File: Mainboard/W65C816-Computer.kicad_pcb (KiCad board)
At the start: 2 copper layers, 93 parts, among them J1 ADDR_DATA_DBG, J2 CTRL_BANK_DBG, J3 CPU_MISC_DBG, J4 PJ-102A, J5 DAUGHTER_PWR_AUX, J6 DAUGHTER_BUS_A, J7 DAUGHTER_BUS_B, Q1 P-MOSFET_REV_PROT_TO220, SW1 RESET, SW2 NMI, SW3 MAIN_PWR_SW_EXT, U1 W65C816S6PG-14, U10 SN74HC04N, U2 SN74HC573N, U20 AS6C4008-55PCN, U21 AS6C4008-55PCN, U22 AS6C4008-55PCN, U23 AS6C4008-55PCN, U24 AS6C4008-55PCN, U25 AS6C4008-55PCN, U26 AS6C4008-55PCN, U27 AS6C4008-55PCN, U3 SN74HC245N, U30 SST39VF040-70-4I-NHE, U4 MCP130-315D, U5 SN74HC14N, U6 SN74HC138N, U7 SN74HC138N, U9 SN74HC00N, X1 ECS-P143X-8.000-BN

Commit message: Add lock file for W65C816-Computer project with hostname and username
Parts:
- moved J6 198.0 mm to (322.2, -24.3)
- moved J7 163.9 mm to (315.0, -24.3)

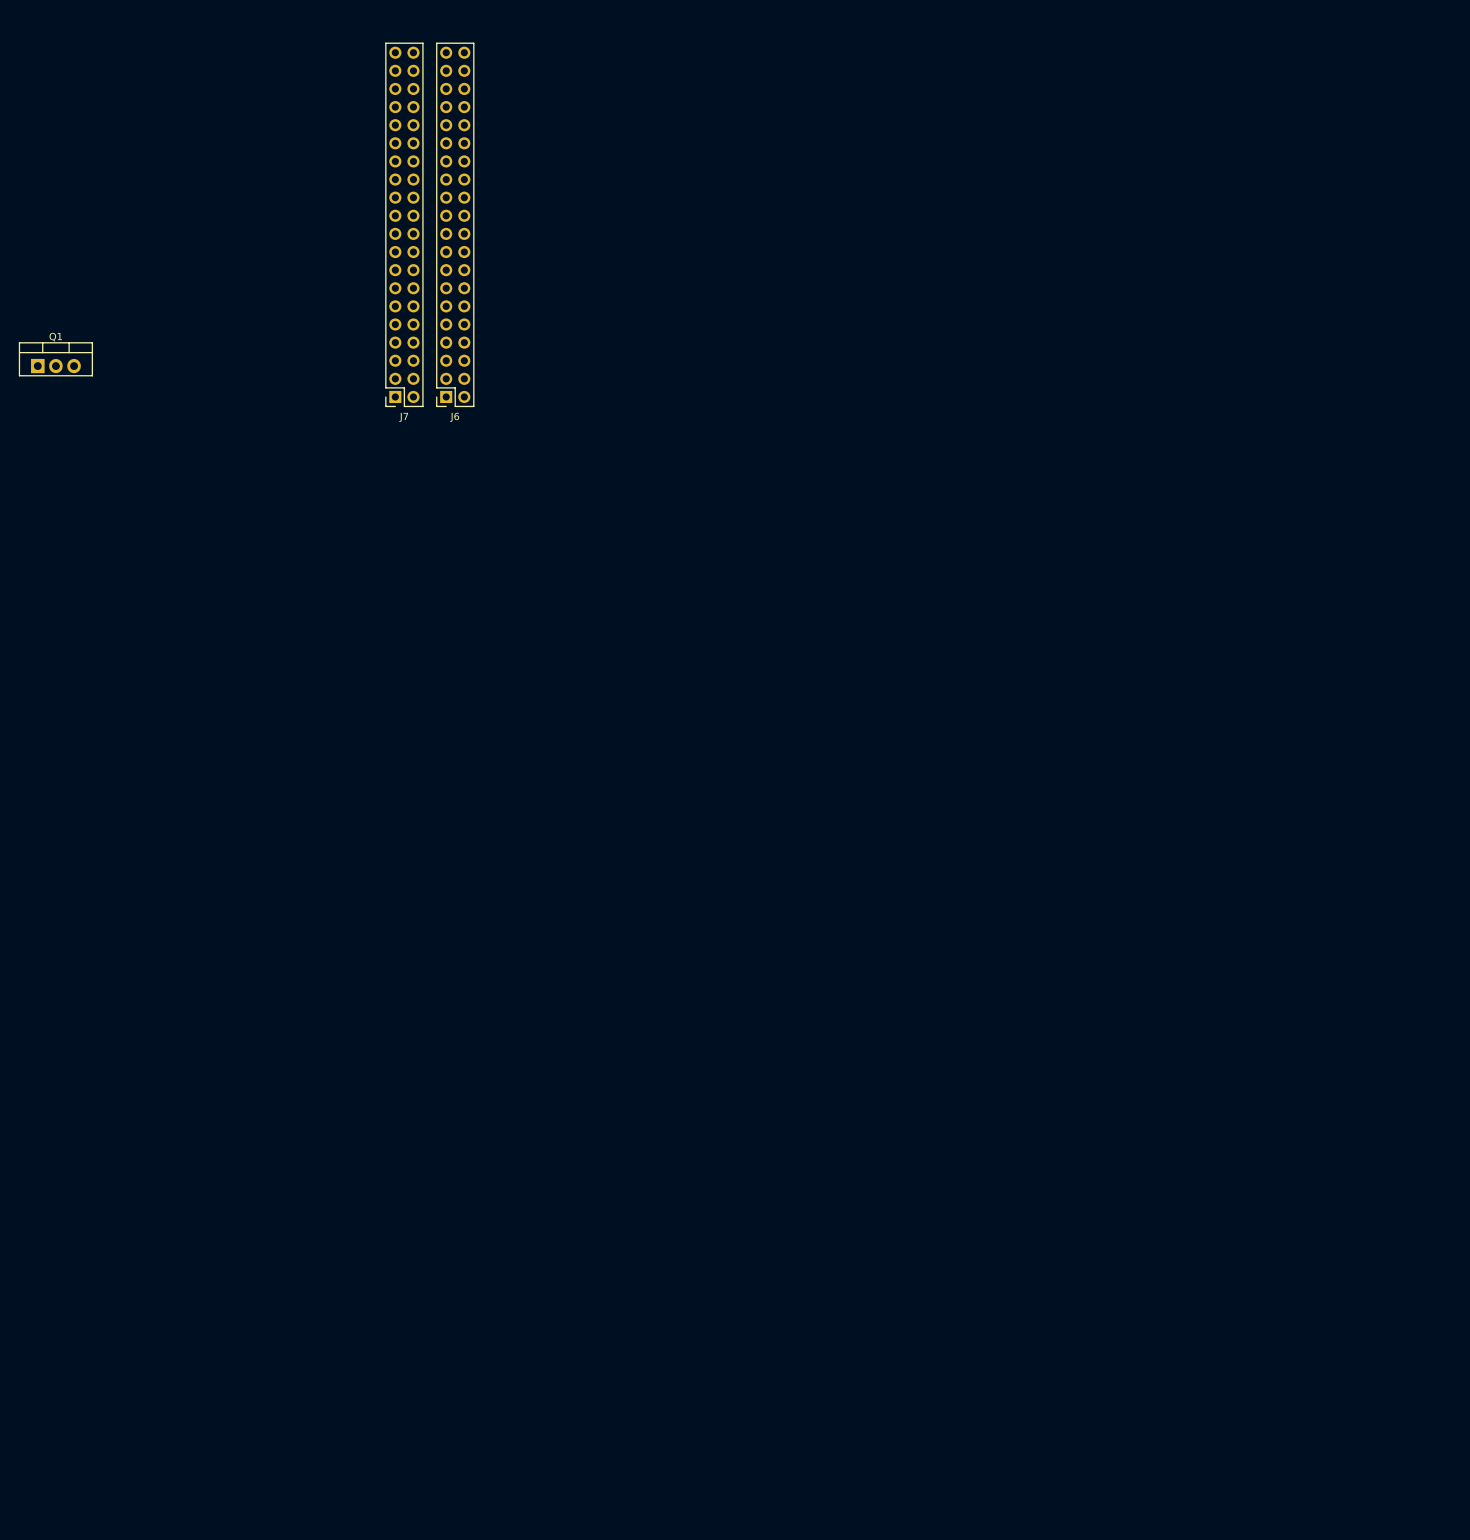
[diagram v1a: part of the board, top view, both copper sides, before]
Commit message: Add CardEdge EDAC 395 footprint and update library table
- Created a new footprint for the CardEdge EDAC 395 2x40 P2.54mm Vertical THT connector in the W65C816-Computer.pretty library.
- Added the footprint to the fp-lib-table for easy access in KiCad.
- Documented the W65C816/RP2350 interface plan, outlining architecture, memory mapping, data bus contracts, interrupt architecture, and implementation sequence for revision A.
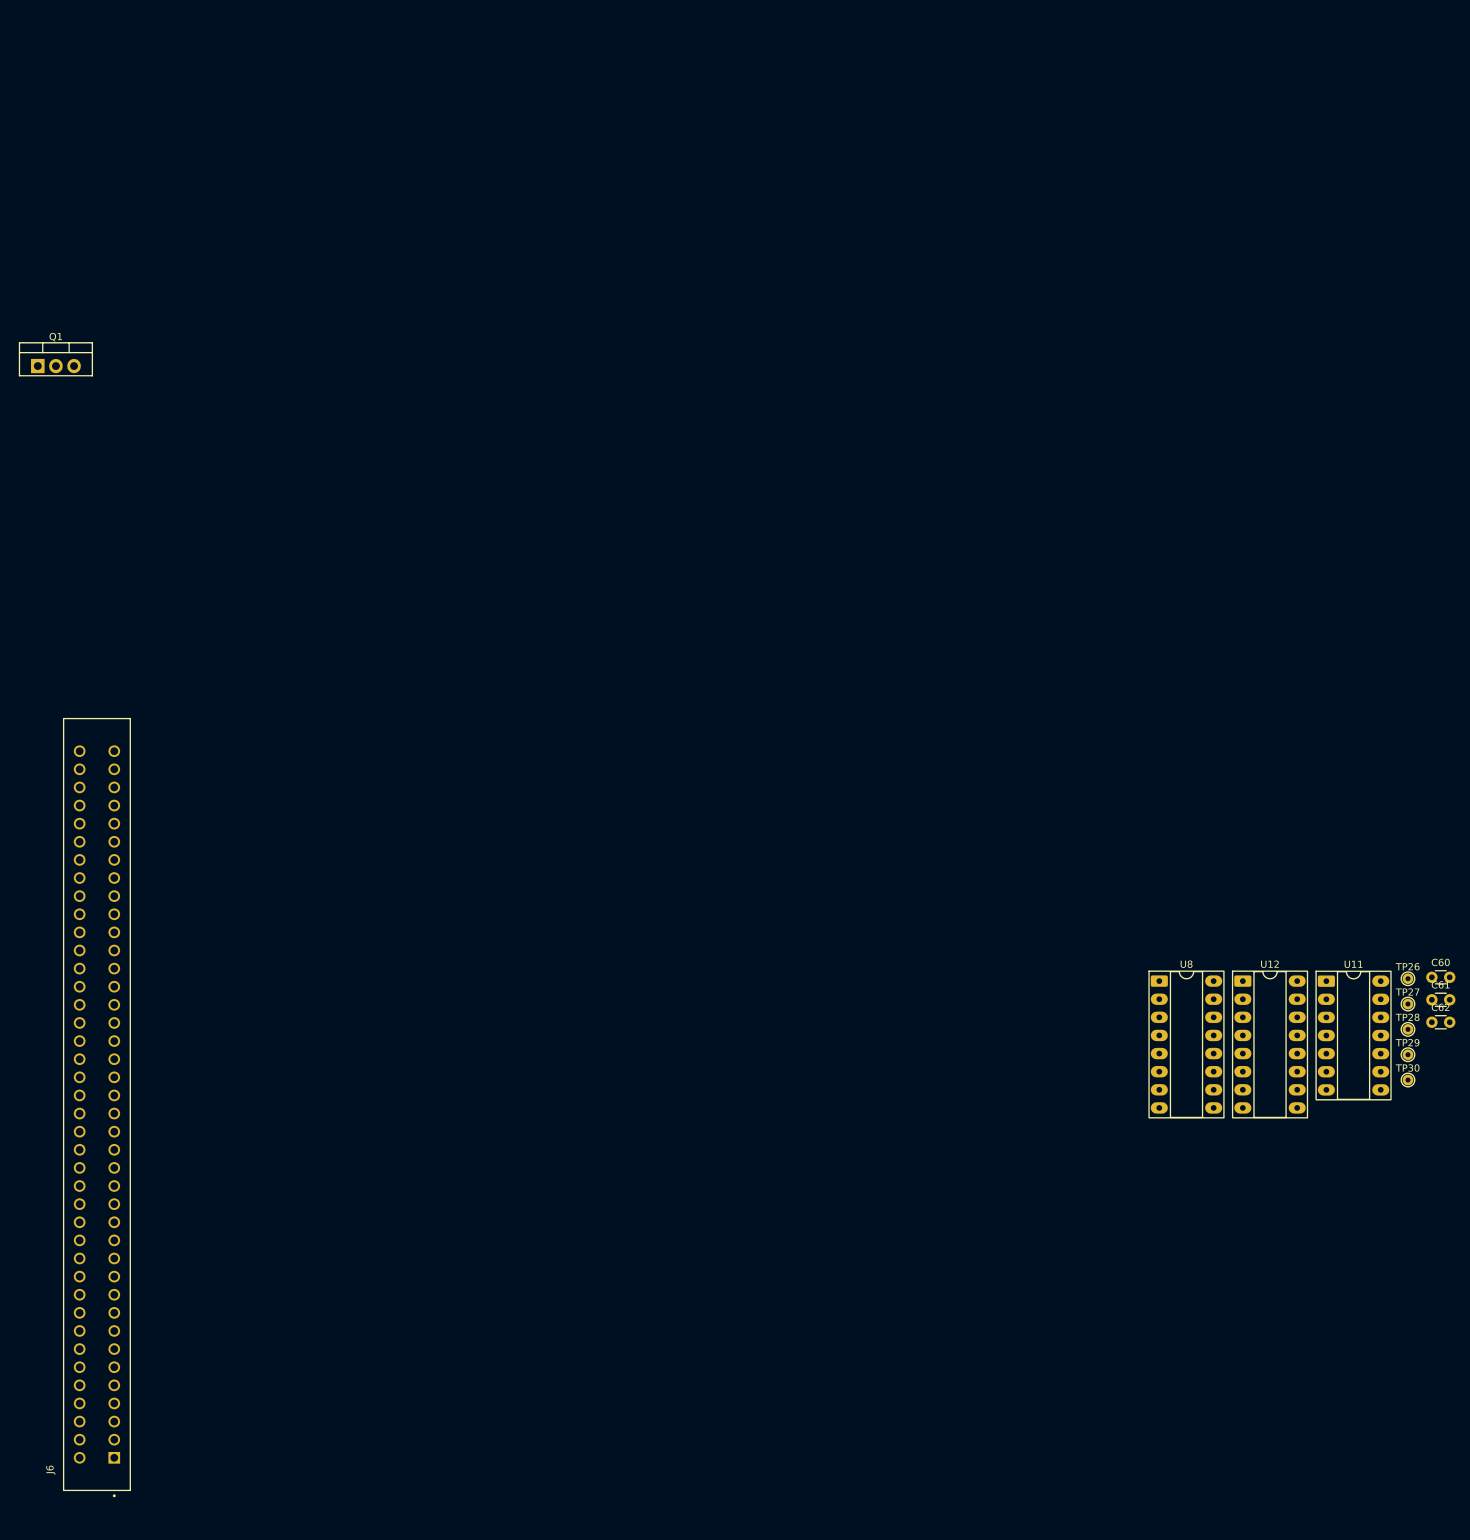
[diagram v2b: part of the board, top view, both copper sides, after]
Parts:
- removed J7: DAUGHTER_BUS_B, Connector_PinSocket_2.54mm:PinSocket_2x20_P2.54mm_Vertical
- added C60: 100nF, Capacitor_THT:C_Disc_D3.0mm_W1.6mm_P2.50mm, F.Cu at (460.4, 57.0)
- added C61: 100nF, Capacitor_THT:C_Disc_D3.0mm_W1.6mm_P2.50mm, F.Cu at (460.4, 60.2)
- added C62: 100nF, Capacitor_THT:C_Disc_D3.0mm_W1.6mm_P2.50mm, F.Cu at (460.4, 63.3)
- added TP26: RP_CS_N, TestPoint:TestPoint_THTPad_D1.5mm_Drill0.7mm, F.Cu at (457.0, 57.2)
- added TP27: IO_CS_N, TestPoint:TestPoint_THTPad_D1.5mm_Drill0.7mm, F.Cu at (457.0, 60.8)
- added TP28: EXP_CS_N, TestPoint:TestPoint_THTPad_D1.5mm_Drill0.7mm, F.Cu at (457.0, 64.3)
- added TP29: IO_RD_N, TestPoint:TestPoint_THTPad_D1.5mm_Drill0.7mm, F.Cu at (457.0, 67.9)
- added TP30: IO_WR_N, TestPoint:TestPoint_THTPad_D1.5mm_Drill0.7mm, F.Cu at (457.0, 71.4)
- added U11: SN74HC08N, Package_DIP:DIP-14_W7.62mm_Socket_LongPads, F.Cu at (445.6, 57.6)
- added U12: SN74HC139N, Package_DIP:DIP-16_W7.62mm_Socket_LongPads, F.Cu at (433.9, 57.6)
- added U8: SN74HC138N, Package_DIP:DIP-16_W7.62mm_Socket_LongPads, F.Cu at (422.1, 57.6)
- J6: value DAUGHTER_BUS_A -> DAUGHTER_CARD_EDGE; footprint Connector_PinSocket_2.54mm:PinSocket_2x20_P2.54mm_Vertical -> 80_Standard_Edge_Conn:TE_2-5530843-0
- moved J6 110.6 mm to (273.2, 74.9), turned to 90 degrees

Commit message: Add ISA16 Slot footprint and mainboard PCB file
- Introduced a new footprint for the ISA16 Slot, including detailed pad specifications and dimensions.
- Added the W65C816-Computer.kicad_pcb.zip file containing the mainboard PCB design.
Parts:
- removed C1, C10, C11, C12, C2, C20, C21, C22, C23, C24, C25, C26, C27, C3, C30, C4, C41, C43, C5, C60, C61, C62, C7, C8, C9: 100nF, Capacitor_THT:C_Disc_D3.0mm_W1.6mm_P2.50mm
- removed C40, C42: 470uF, Capacitor_THT:CP_Radial_D8.0mm_P5.00mm
- removed C6: 10uF, Capacitor_THT:C_Disc_D5.0mm_W2.5mm_P2.50mm
- removed D1: P6KE5.0A, Diode_THT:D_DO-15_P10.16mm_Horizontal
- removed F1: 5A, Fuse:Fuseholder_Clip-5x20mm_Littelfuse_111_Inline_P20.00x5.00mm_D1.05mm_Horizontal
- removed J1: ADDR_DATA_DBG, Connector_PinHeader_2.54mm:PinHeader_1x20_P2.54mm_Vertical
- removed J2: CTRL_BANK_DBG, Connector_PinHeader_2.54mm:PinHeader_1x20_P2.54mm_Vertical
- removed J3: CPU_MISC_DBG, Connector_PinHeader_2.54mm:PinHeader_1x10_P2.54mm_Vertical
- removed J4: PJ-102A, PJ-102A:CUI_PJ-102A
- removed J5: DAUGHTER_PWR_AUX, Connector_PinSocket_2.54mm:PinSocket_1x06_P2.54mm_Vertical
- removed J6: DAUGHTER_CARD_EDGE, 80_Standard_Edge_Conn:TE_2-5530843-0
- removed JP1: FLASH_WE_EN, Connector_PinHeader_2.54mm:PinHeader_1x02_P2.54mm_Vertical
- removed LED1: PWR, LED_THT:LED_D5.0mm
- removed MOD1: 3V3_BUCK_MODULE_5V_IN_3A, Connector_PinSocket_2.54mm:PinSocket_1x04_P2.54mm_Vertical
- removed Q1: P-MOSFET_REV_PROT_TO220, Package_TO_SOT_THT:TO-220-3_Vertical
- removed R1, R2, R3, R30, R4, R5, R6: 10k, Resistor_THT:R_Axial_DIN0207_L6.3mm_D2.5mm_P7.62mm_Horizontal
- removed R41: 1k, Resistor_THT:R_Axial_DIN0207_L6.3mm_D2.5mm_P7.62mm_Horizontal
- removed SW1: RESET, Button_Switch_THT:SW_PUSH_6mm_H4.3mm
- removed SW2: NMI, Button_Switch_THT:SW_PUSH_6mm_H4.3mm
- removed SW3: MAIN_PWR_SW_EXT, TerminalBlock_RND:TerminalBlock_RND_205-00232_1x02_P5.08mm_Horizontal
- removed TP1: PHI2, TestPoint:TestPoint_THTPad_D1.5mm_Drill0.7mm
- removed TP10: ABORT_N, TestPoint:TestPoint_THTPad_D1.5mm_Drill0.7mm
- removed TP11: PHI2_N, TestPoint:TestPoint_THTPad_D1.5mm_Drill0.7mm
- removed TP12: RAM_CS0_N, TestPoint:TestPoint_THTPad_D1.5mm_Drill0.7mm
- removed TP13: RAM_CS1_N, TestPoint:TestPoint_THTPad_D1.5mm_Drill0.7mm
- removed TP14: RAM_CS2_N, TestPoint:TestPoint_THTPad_D1.5mm_Drill0.7mm
- removed TP15: RAM_CS3_N, TestPoint:TestPoint_THTPad_D1.5mm_Drill0.7mm
- removed TP16: RAM_CS4_N, TestPoint:TestPoint_THTPad_D1.5mm_Drill0.7mm
- removed TP17: RAM_CS5_N, TestPoint:TestPoint_THTPad_D1.5mm_Drill0.7mm
- removed TP18: RAM_CS6_N, TestPoint:TestPoint_THTPad_D1.5mm_Drill0.7mm
- removed TP19: RAM_CS7_N, TestPoint:TestPoint_THTPad_D1.5mm_Drill0.7mm
- removed TP2: RESET_N, TestPoint:TestPoint_THTPad_D1.5mm_Drill0.7mm
- removed TP20: ROM_CS_N, TestPoint:TestPoint_THTPad_D1.5mm_Drill0.7mm
- removed TP21: MEM_OE_N, TestPoint:TestPoint_THTPad_D1.5mm_Drill0.7mm
- removed TP22: MEM_WE_N, TestPoint:TestPoint_THTPad_D1.5mm_Drill0.7mm
- removed TP23: +5V, TestPoint:TestPoint_THTPad_D1.5mm_Drill0.7mm
- removed TP24: +3V3, TestPoint:TestPoint_THTPad_D1.5mm_Drill0.7mm
- removed TP25: GND, TestPoint:TestPoint_THTPad_D1.5mm_Drill0.7mm
- removed TP26: RP_CS_N, TestPoint:TestPoint_THTPad_D1.5mm_Drill0.7mm
- removed TP27: IO_CS_N, TestPoint:TestPoint_THTPad_D1.5mm_Drill0.7mm
- removed TP28: EXP_CS_N, TestPoint:TestPoint_THTPad_D1.5mm_Drill0.7mm
- removed TP29: IO_RD_N, TestPoint:TestPoint_THTPad_D1.5mm_Drill0.7mm
- removed TP3: IRQ_N, TestPoint:TestPoint_THTPad_D1.5mm_Drill0.7mm
- removed TP30: IO_WR_N, TestPoint:TestPoint_THTPad_D1.5mm_Drill0.7mm
- removed TP4: NMI_N, TestPoint:TestPoint_THTPad_D1.5mm_Drill0.7mm
- removed TP5: RDY, TestPoint:TestPoint_THTPad_D1.5mm_Drill0.7mm
- removed TP6: RWB, TestPoint:TestPoint_THTPad_D1.5mm_Drill0.7mm
- removed TP7: VDA, TestPoint:TestPoint_THTPad_D1.5mm_Drill0.7mm
- removed TP8: VPA, TestPoint:TestPoint_THTPad_D1.5mm_Drill0.7mm
- removed TP9: BE, TestPoint:TestPoint_THTPad_D1.5mm_Drill0.7mm
- removed U1: W65C816S6PG-14, Package_DIP:DIP-40_W15.24mm_Socket_LongPads
- removed U10: SN74HC04N, Package_DIP:DIP-14_W7.62mm_Socket_LongPads
- removed U11: SN74HC08N, Package_DIP:DIP-14_W7.62mm_Socket_LongPads
- removed U12: SN74HC139N, Package_DIP:DIP-16_W7.62mm_Socket_LongPads
- removed U2: SN74HC573N, Package_DIP:DIP-20_W7.62mm_Socket_LongPads
- removed U20, U21, U22, U23, U24, U25, U26, U27: AS6C4008-55PCN, Package_DIP:DIP-32_W15.24mm_Socket_LongPads
- removed U3: SN74HC245N, Package_DIP:DIP-20_W7.62mm_Socket_LongPads
- removed U30: SST39VF040-70-4I-NHE, Package_LCC:PLCC-32_THT-Socket
- removed U4: MCP130-315D, Package_TO_SOT_THT:TO-92_Inline
- removed U5: SN74HC14N, Package_DIP:DIP-14_W7.62mm_Socket_LongPads
- removed U6, U7, U8: SN74HC138N, Package_DIP:DIP-16_W7.62mm_Socket_LongPads
- removed U9: SN74HC00N, Package_DIP:DIP-14_W7.62mm_Socket_LongPads
- removed X1: ECS-P143X-8.000-BN, Oscillator:Oscillator_DIP-14
- added H1: MountingHole, MountingHole:MountingHole_4.3mm_M4_Pad_Via, F.Cu at (32.7, 183.7)
- added H2: MountingHole, MountingHole:MountingHole_4.3mm_M4_Pad_Via, F.Cu at (187.7, 183.7)
- added H3: MountingHole, MountingHole:MountingHole_4.3mm_M4_Pad_Via, F.Cu at (187.7, 26.2)
- added H4: MountingHole, MountingHole:MountingHole_4.3mm_M4_Pad_Via, F.Cu at (55.6, 26.2)
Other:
- board outline added: 170 x 170 mm
- board text added: "@Sulfuroid"
- board text added: "BACK"
- board text added: "MINI-ITX Kicad Template"

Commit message: Added 4MiB memory back
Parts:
- added C1: 100nF, Capacitor_THT:C_Disc_D3.0mm_W1.6mm_P2.50mm, F.Cu at (338.2, -90.4)
- added C10: 100nF, Capacitor_THT:C_Disc_D3.0mm_W1.6mm_P2.50mm, F.Cu at (343.9, -87.3)
- added C11: 100nF, Capacitor_THT:C_Disc_D3.0mm_W1.6mm_P2.50mm, F.Cu at (343.9, -84.1)
- added C12: 100nF, Capacitor_THT:C_Disc_D3.0mm_W1.6mm_P2.50mm, F.Cu at (343.9, -81.0)
- added C2: 100nF, Capacitor_THT:C_Disc_D3.0mm_W1.6mm_P2.50mm, F.Cu at (338.2, -87.3)
- added C20: 100nF, Capacitor_THT:C_Disc_D3.0mm_W1.6mm_P2.50mm, F.Cu at (343.9, -77.8)
- added C21: 100nF, Capacitor_THT:C_Disc_D3.0mm_W1.6mm_P2.50mm, F.Cu at (343.9, -74.7)
- added C22: 100nF, Capacitor_THT:C_Disc_D3.0mm_W1.6mm_P2.50mm, F.Cu at (343.9, -71.5)
- added C23: 100nF, Capacitor_THT:C_Disc_D3.0mm_W1.6mm_P2.50mm, F.Cu at (349.5, -90.4)
- added C24: 100nF, Capacitor_THT:C_Disc_D3.0mm_W1.6mm_P2.50mm, F.Cu at (294.3, -14.2)
- added C25: 100nF, Capacitor_THT:C_Disc_D3.0mm_W1.6mm_P2.50mm, F.Cu at (349.5, -84.1)
- added C26: 100nF, Capacitor_THT:C_Disc_D3.0mm_W1.6mm_P2.50mm, F.Cu at (349.5, -81.0)
- added C27: 100nF, Capacitor_THT:C_Disc_D3.0mm_W1.6mm_P2.50mm, F.Cu at (349.5, -77.8)
- added C3: 100nF, Capacitor_THT:C_Disc_D3.0mm_W1.6mm_P2.50mm, F.Cu at (338.2, -84.1)
- added C30: 100nF, Capacitor_THT:C_Disc_D3.0mm_W1.6mm_P2.50mm, F.Cu at (349.5, -74.7)
- added C4: 100nF, Capacitor_THT:C_Disc_D3.0mm_W1.6mm_P2.50mm, F.Cu at (338.2, -81.0)
- added C40: 470uF, Capacitor_THT:CP_Radial_D8.0mm_P5.00mm, F.Cu at (361.7, -87.2)
- added C41: 100nF, Capacitor_THT:C_Disc_D3.0mm_W1.6mm_P2.50mm, F.Cu at (349.5, -71.5)
- added C42: 470uF, Capacitor_THT:CP_Radial_D8.0mm_P5.00mm, F.Cu at (361.7, -77.7)
- added C43: 100nF, Capacitor_THT:C_Disc_D3.0mm_W1.6mm_P2.50mm, F.Cu at (355.2, -90.4)
- added C5: 100nF, Capacitor_THT:C_Disc_D3.0mm_W1.6mm_P2.50mm, F.Cu at (338.2, -77.8)
- added C6: 10uF, Capacitor_THT:C_Disc_D5.0mm_W2.5mm_P2.50mm, F.Cu at (363.5, -37.8)
- added C60: 100nF, Capacitor_THT:C_Disc_D3.0mm_W1.6mm_P2.50mm, F.Cu at (355.2, -87.3)
- added C61: 100nF, Capacitor_THT:C_Disc_D3.0mm_W1.6mm_P2.50mm, F.Cu at (355.2, -84.1)
- added C62: 100nF, Capacitor_THT:C_Disc_D3.0mm_W1.6mm_P2.50mm, F.Cu at (355.2, -81.0)
- added C7: 100nF, Capacitor_THT:C_Disc_D3.0mm_W1.6mm_P2.50mm, F.Cu at (338.2, -74.7)
- added C8: 100nF, Capacitor_THT:C_Disc_D3.0mm_W1.6mm_P2.50mm, F.Cu at (338.2, -71.5)
- added C9: 100nF, Capacitor_THT:C_Disc_D3.0mm_W1.6mm_P2.50mm, F.Cu at (343.9, -90.4)
- added D1: P6KE5.0A, Diode_THT:D_DO-15_P10.16mm_Horizontal, F.Cu at (349.4, -44.7)
- added F1: 5A, Fuse:Fuseholder_Clip-5x20mm_Littelfuse_111_Inline_P20.00x5.00mm_D1.05mm_Horizontal, F.Cu at (279.3, -41.3)
- added J1: ADDR_DATA_DBG, Connector_PinHeader_2.54mm:PinHeader_1x20_P2.54mm_Vertical, F.Cu at (329.7, -116.7)
- added J2: CTRL_BANK_DBG, Connector_PinHeader_2.54mm:PinHeader_1x20_P2.54mm_Vertical, F.Cu at (334.3, -116.7)
- added J3: CPU_MISC_DBG, Connector_PinHeader_2.54mm:PinHeader_1x10_P2.54mm_Vertical, F.Cu at (329.7, -63.9)
- added J4: PJ-102A, PJ-102A:CUI_PJ-102A, F.Cu at (314.6, -55.0)
- added J5: DAUGHTER_PWR_AUX, Connector_PinSocket_2.54mm:PinSocket_1x06_P2.54mm_Vertical, F.Cu at (334.3, -63.9)
- added J6: ISA16_DAUGHTER_BUS, W65C816_Connector:ISA16_Slot, F.Cu at (110.6, 181.4)
- added JP1: FLASH_WE_EN, Connector_PinHeader_2.54mm:PinHeader_1x02_P2.54mm_Vertical, F.Cu at (303.4, -42.4)
- added LED1: PWR, LED_THT:LED_D5.0mm, F.Cu at (364.0, -43.5)
- added MOD1: 3V3_BUCK_MODULE_5V_IN_3A, Connector_PinSocket_2.54mm:PinSocket_1x04_P2.54mm_Vertical, F.Cu at (322.6, -47.7)
- added Q1: P-MOSFET_REV_PROT_TO220, Package_TO_SOT_THT:TO-220-3_Vertical, F.Cu at (350.6, -38.2)
- added R1: 10k, Resistor_THT:R_Axial_DIN0207_L6.3mm_D2.5mm_P7.62mm_Horizontal, F.Cu at (338.2, -67.9)
- added R2: 10k, Resistor_THT:R_Axial_DIN0207_L6.3mm_D2.5mm_P7.62mm_Horizontal, F.Cu at (338.2, -63.9)
- added R3: 10k, Resistor_THT:R_Axial_DIN0207_L6.3mm_D2.5mm_P7.62mm_Horizontal, F.Cu at (338.2, -59.8)
- added R30: 10k, Resistor_THT:R_Axial_DIN0207_L6.3mm_D2.5mm_P7.62mm_Horizontal, F.Cu at (338.2, -43.6)
- added R4: 10k, Resistor_THT:R_Axial_DIN0207_L6.3mm_D2.5mm_P7.62mm_Horizontal, F.Cu at (338.2, -55.8)
- added R41: 1k, Resistor_THT:R_Axial_DIN0207_L6.3mm_D2.5mm_P7.62mm_Horizontal, F.Cu at (338.2, -39.6)
- added R5: 10k, Resistor_THT:R_Axial_DIN0207_L6.3mm_D2.5mm_P7.62mm_Horizontal, F.Cu at (338.2, -51.7)
- added R6: 10k, Resistor_THT:R_Axial_DIN0207_L6.3mm_D2.5mm_P7.62mm_Horizontal, F.Cu at (338.2, -47.7)
- added SW1: RESET, Button_Switch_THT:SW_PUSH_6mm_H4.3mm, F.Cu at (362.1, -117.0)
- added SW2: NMI, Button_Switch_THT:SW_PUSH_6mm_H4.3mm, F.Cu at (362.1, -108.5)
- added SW3: MAIN_PWR_SW_EXT, TerminalBlock_RND:TerminalBlock_RND_205-00232_1x02_P5.08mm_Horizontal, F.Cu at (311.7, -44.6)
- added TP1: PHI2, TestPoint:TestPoint_THTPad_D1.5mm_Drill0.7mm, F.Cu at (279.3, -74.9)
- added TP10: ABORT_N, TestPoint:TestPoint_THTPad_D1.5mm_Drill0.7mm, F.Cu at (282.9, -60.7)
- added TP11: PHI2_N, TestPoint:TestPoint_THTPad_D1.5mm_Drill0.7mm, F.Cu at (286.4, -74.9)
- added TP12: RAM_CS0_N, TestPoint:TestPoint_THTPad_D1.5mm_Drill0.7mm, F.Cu at (286.4, -71.4)
- added TP13: RAM_CS1_N, TestPoint:TestPoint_THTPad_D1.5mm_Drill0.7mm, F.Cu at (286.4, -67.8)
- added TP14: RAM_CS2_N, TestPoint:TestPoint_THTPad_D1.5mm_Drill0.7mm, F.Cu at (286.4, -64.3)
- added TP15: RAM_CS3_N, TestPoint:TestPoint_THTPad_D1.5mm_Drill0.7mm, F.Cu at (286.4, -60.7)
- added TP16: RAM_CS4_N, TestPoint:TestPoint_THTPad_D1.5mm_Drill0.7mm, F.Cu at (290.0, -74.9)
- added TP17: RAM_CS5_N, TestPoint:TestPoint_THTPad_D1.5mm_Drill0.7mm, F.Cu at (290.0, -71.4)
- added TP18: RAM_CS6_N, TestPoint:TestPoint_THTPad_D1.5mm_Drill0.7mm, F.Cu at (290.0, -67.8)
- added TP19: RAM_CS7_N, TestPoint:TestPoint_THTPad_D1.5mm_Drill0.7mm, F.Cu at (290.0, -64.3)
- added TP2: RESET_N, TestPoint:TestPoint_THTPad_D1.5mm_Drill0.7mm, F.Cu at (279.3, -71.4)
- added TP20: ROM_CS_N, TestPoint:TestPoint_THTPad_D1.5mm_Drill0.7mm, F.Cu at (290.0, -60.7)
- added TP21: MEM_OE_N, TestPoint:TestPoint_THTPad_D1.5mm_Drill0.7mm, F.Cu at (293.5, -74.9)
- added TP22: MEM_WE_N, TestPoint:TestPoint_THTPad_D1.5mm_Drill0.7mm, F.Cu at (293.5, -71.4)
- added TP23: +5V, TestPoint:TestPoint_THTPad_D1.5mm_Drill0.7mm, F.Cu at (293.5, -67.8)
- added TP24: +3V3, TestPoint:TestPoint_THTPad_D1.5mm_Drill0.7mm, F.Cu at (293.5, -64.3)
- added TP25: GND, TestPoint:TestPoint_THTPad_D1.5mm_Drill0.7mm, F.Cu at (293.5, -60.7)
- added TP26: RP_CS_N, TestPoint:TestPoint_THTPad_D1.5mm_Drill0.7mm, F.Cu at (297.1, -74.9)
- added TP27: IO_CS_N, TestPoint:TestPoint_THTPad_D1.5mm_Drill0.7mm, F.Cu at (297.1, -71.4)
- added TP28: EXP_CS_N, TestPoint:TestPoint_THTPad_D1.5mm_Drill0.7mm, F.Cu at (297.1, -67.8)
- added TP29: IO_RD_N, TestPoint:TestPoint_THTPad_D1.5mm_Drill0.7mm, F.Cu at (297.1, -64.3)
- added TP3: IRQ_N, TestPoint:TestPoint_THTPad_D1.5mm_Drill0.7mm, F.Cu at (279.3, -67.8)
- added TP30: IO_WR_N, TestPoint:TestPoint_THTPad_D1.5mm_Drill0.7mm, F.Cu at (297.1, -60.7)
- added TP4: NMI_N, TestPoint:TestPoint_THTPad_D1.5mm_Drill0.7mm, F.Cu at (279.3, -64.3)
- added TP5: RDY, TestPoint:TestPoint_THTPad_D1.5mm_Drill0.7mm, F.Cu at (279.3, -60.7)
- added TP6: RWB, TestPoint:TestPoint_THTPad_D1.5mm_Drill0.7mm, F.Cu at (282.9, -74.9)
- added TP7: VDA, TestPoint:TestPoint_THTPad_D1.5mm_Drill0.7mm, F.Cu at (282.9, -71.4)
- added TP8: VPA, TestPoint:TestPoint_THTPad_D1.5mm_Drill0.7mm, F.Cu at (282.9, -67.8)
- added TP9: BE, TestPoint:TestPoint_THTPad_D1.5mm_Drill0.7mm, F.Cu at (282.9, -64.3)
- added U1: W65C816S6PG-14, Package_DIP:DIP-40_W15.24mm_Socket_LongPads, F.Cu at (134.7, 83.7)
- added U10: SN74HC04N, Package_DIP:DIP-14_W7.62mm_Socket_LongPads, F.Cu at (256.2, -52.6)
- added U11: SN74HC08N, Package_DIP:DIP-14_W7.62mm_Socket_LongPads, F.Cu at (267.9, -52.6)
- added U12: SN74HC139N, Package_DIP:DIP-16_W7.62mm_Socket_LongPads, F.Cu at (267.9, -74.6)
- added U2: SN74HC573N, Package_DIP:DIP-20_W7.62mm_Socket_LongPads, F.Cu at (338.7, -116.9)
- added U20: AS6C4008-55PCN, Package_DIP:DIP-32_W15.24mm_Socket_LongPads, F.Cu at (129.7, 107.8)
- added U21: AS6C4008-55PCN, Package_DIP:DIP-32_W15.24mm_Socket_LongPads, F.Cu at (129.7, 127.2)
- added U22: AS6C4008-55PCN, Package_DIP:DIP-32_W15.24mm_Socket_LongPads, F.Cu at (129.4, 39.6)
- added U23: AS6C4008-55PCN, Package_DIP:DIP-32_W15.24mm_Socket_LongPads, F.Cu at (129.4, 58.9)
- added U24: AS6C4008-55PCN, Package_DIP:DIP-32_W15.24mm_Socket_LongPads, F.Cu at (183.2, 39.1)
- added U25: AS6C4008-55PCN, Package_DIP:DIP-32_W15.24mm_Socket_LongPads, F.Cu at (183.2, 59.0)
- added U26: AS6C4008-55PCN, Package_DIP:DIP-32_W15.24mm_Socket_LongPads, F.Cu at (183.2, 107.4)
- added U27: AS6C4008-55PCN, Package_DIP:DIP-32_W15.24mm_Socket_LongPads, F.Cu at (183.2, 127.4)
- added U3: SN74HC245N, Package_DIP:DIP-20_W7.62mm_Socket_LongPads, F.Cu at (350.4, -116.9)
- added U30: SST39VF040-70-4I-NHE, Package_LCC:PLCC-32_THT-Socket, F.Cu at (72.1, 92.2)
- added U4: MCP130-315D, Package_TO_SOT_THT:TO-92_Inline, F.Cu at (362.0, -98.7)
- added U5: SN74HC14N, Package_DIP:DIP-14_W7.62mm_Socket_LongPads, F.Cu at (232.7, -52.6)
- added U6: SN74HC138N, Package_DIP:DIP-16_W7.62mm_Socket_LongPads, F.Cu at (232.7, -74.6)
- added U7: SN74HC138N, Package_DIP:DIP-16_W7.62mm_Socket_LongPads, F.Cu at (244.5, -74.6)
- added U8: SN74HC138N, Package_DIP:DIP-16_W7.62mm_Socket_LongPads, F.Cu at (256.2, -74.6)
- added U9: SN74HC00N, Package_DIP:DIP-14_W7.62mm_Socket_LongPads, F.Cu at (244.5, -52.6)
- added X1: ECS-P143X-8.000-BN, Oscillator:Oscillator_DIP-14, F.Cu at (141.0, 95.1)
